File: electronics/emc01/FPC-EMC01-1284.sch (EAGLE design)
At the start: 75 parts, among them J1 USB-MINIB-5PIN, J11 CONN-RECT-16PIN-2ROW, J12 CONN-RECT-16PIN-2ROW, J13 CONN-RECT-16PIN-2ROW, J14 CONN-RECT-16PIN-2ROW, J15 DNP, J16 ICSP, J2 CONN-MOLEX-MICROFIT-6PIN, J3 DNP, J4A MOT-X, J5A MOT-Y, J6A MOT-Z, J7A CONN-RECT-3PINJST_PH_2MM, J8A CONN-RECT-3PINJST_PH_2MM, J9A CONN-RECT-3PINJST_PH_2MM, Q2 2N7002PW, U1 IC-ATMEGA1284P-AU, U2 FT231XS, X1 16Mhz

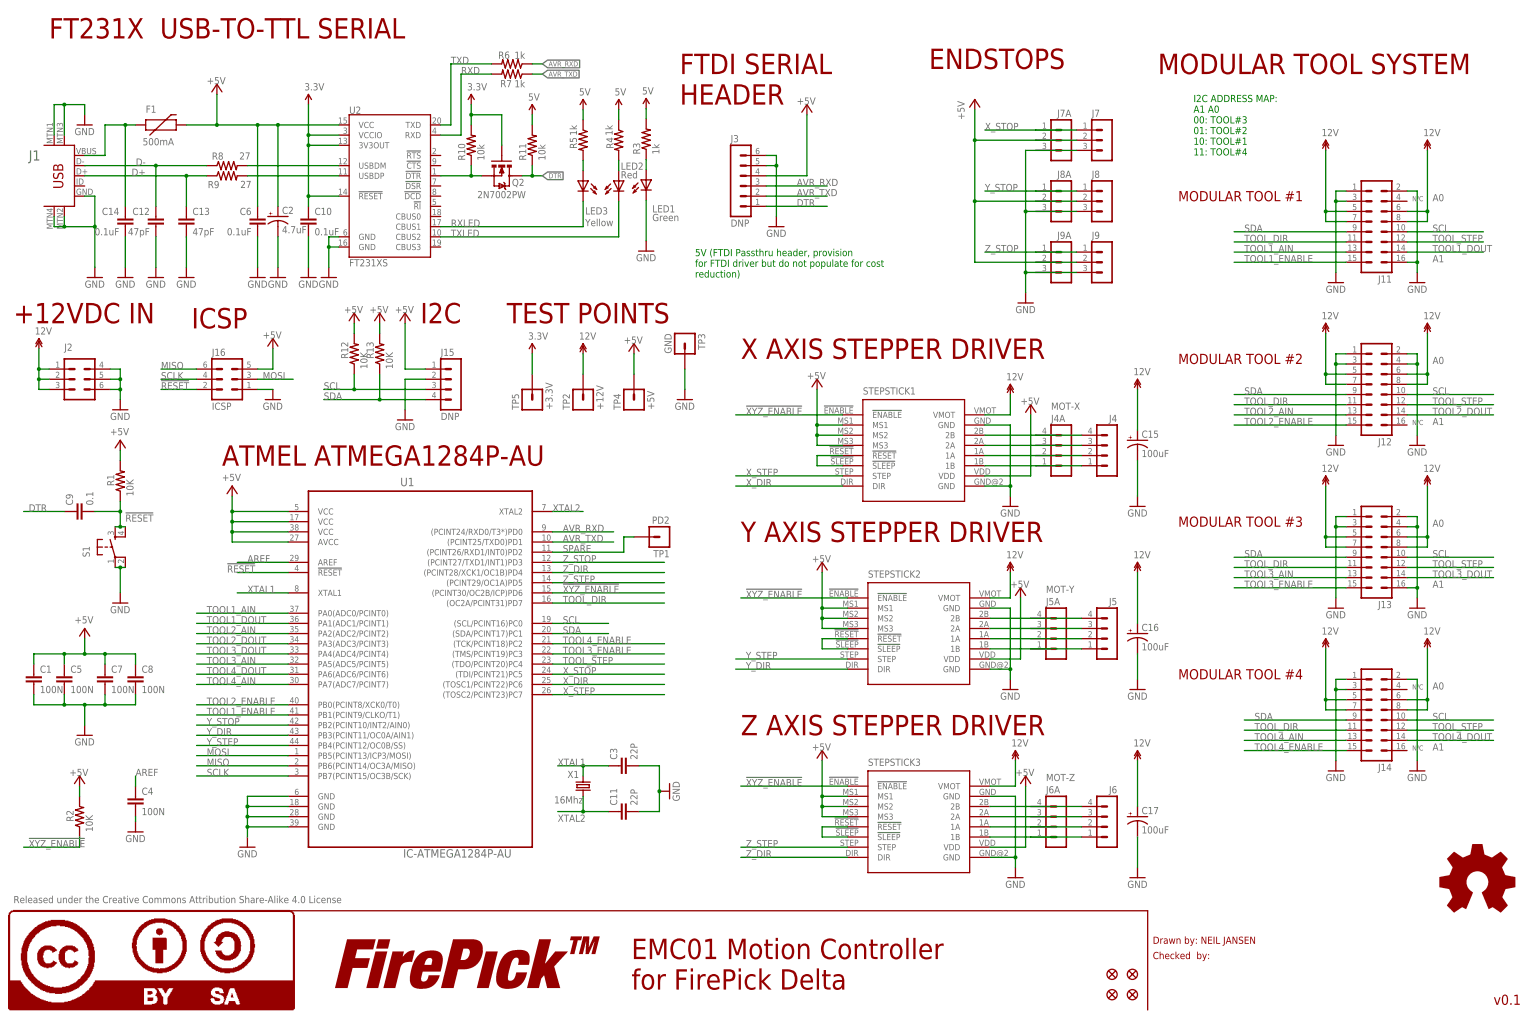
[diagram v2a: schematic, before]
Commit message: Updated all EAGLE PCB's for first Prototype production run.
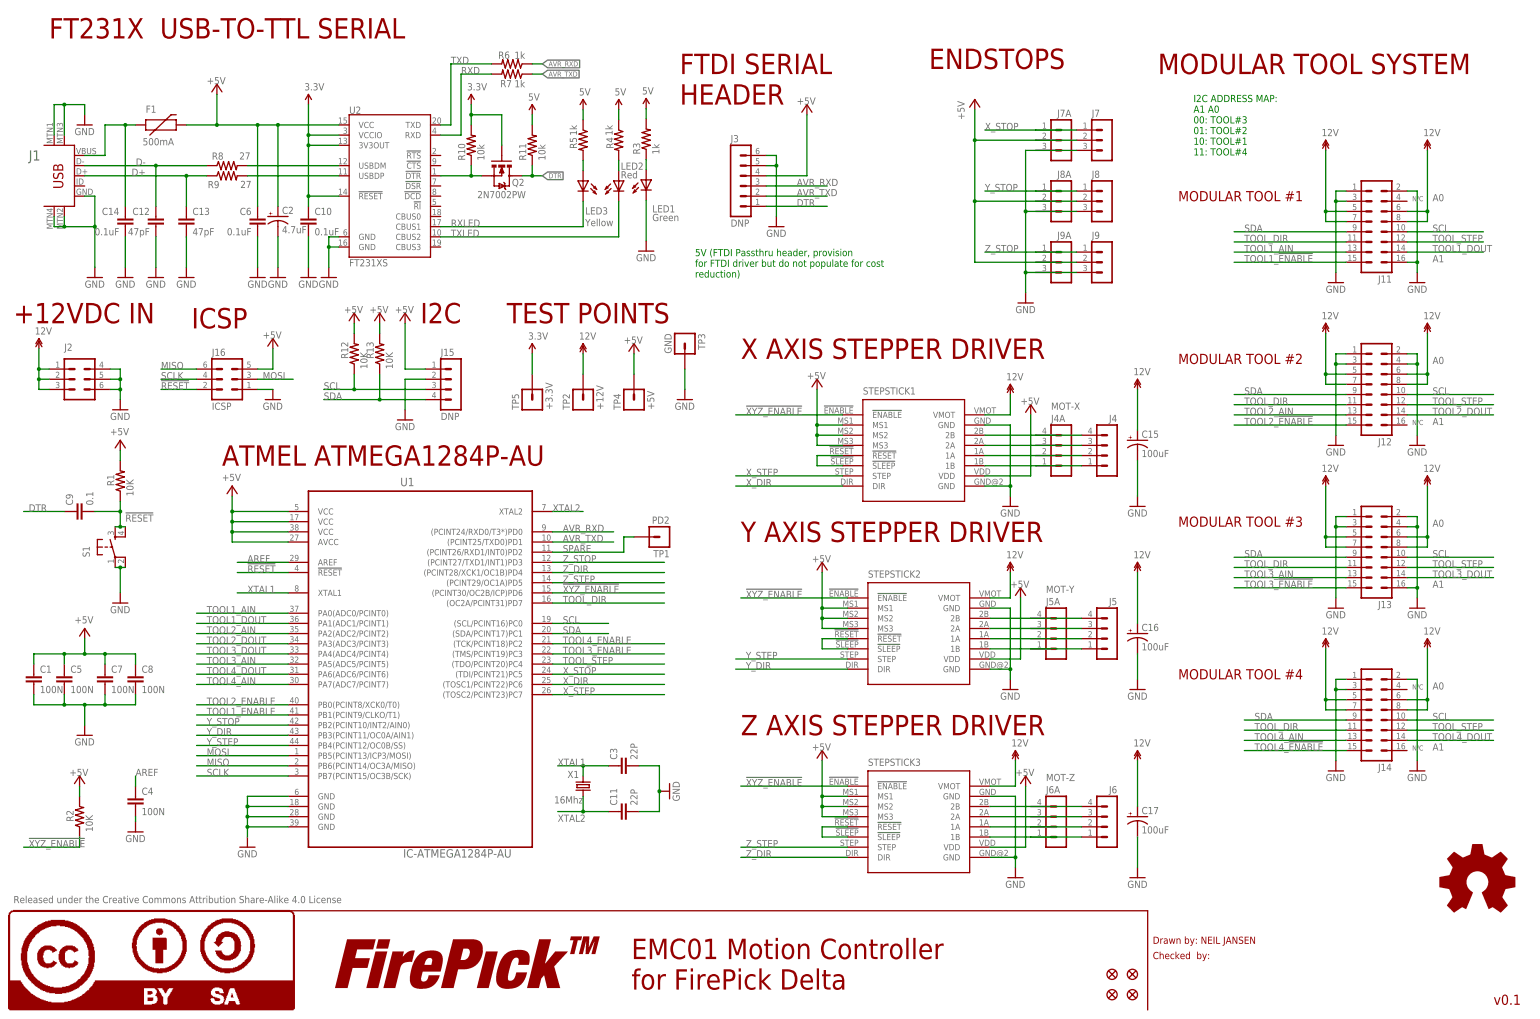
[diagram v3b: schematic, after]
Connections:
- new net TOOL1_!ENABLE: J11.15
- new net TOOL2_!ENABLE: J12.15
- new net TOOL3_!ENABLE: J13.15
- new net TOOL4_!ENABLE: J14.15
- net TOOL1_ENABLE: no longer J11.15
- net TOOL2_ENABLE: no longer J12.15
- net TOOL3_ENABLE: no longer J13.15
- net TOOL4_ENABLE: no longer J14.15
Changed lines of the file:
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@@
 <setting verticaltext="up"/>
 </settings>
-<grid distance="0.05" unitdist="inch" unit="inch" style="lines" multiple="1" display="no" altdistance="0.01" altunitdist="inch" altunit="inch"/>
+<grid distance="0.1" unitdist="inch" unit="inch" style="lines" multiple="1" display="no" altdistance="0.01" altunitdist="inch" altunit="inch"/>
 <layers>
 <layer number="1" name="Top" color="4" fill="1" visible="no" active="no"/>
@@
 <net name="TOOL1_ENABLE" class="0">
 <segment>
-<pinref part="J11" gate="G$1" pin="15"/>
-<wire x1="309.88" y1="190.5" x2="337.82" y2="190.5" width="0.1524" layer="91"/>
-<label x="312.42" y="190.5" size="1.778" layer="95"/>
-</segment>
-<segment>
 <pinref part="U1" gate="G$1" pin="PB1(PCINT9/CLKO/T1)"/>
 <wire x1="50.8" y1="77.47" x2="73.66" y2="77.47" width="0.1524" layer="91"/>
@@
 <net name="TOOL2_ENABLE" class="0">
 <segment>
-<pinref part="J12" gate="G$1" pin="15"/>
-<wire x1="337.82" y1="149.86" x2="309.88" y2="149.86" width="0.1524" layer="91"/>
-<label x="312.42" y="149.86" size="1.778" layer="95"/>
-</segment>
-<segment>
 <pinref part="U1" gate="G$1" pin="PB0(PCINT8/XCK0/T0)"/>
 <wire x1="73.66" y1="80.01" x2="50.8" y2="80.01" width="0.1524" layer="91"/>
@@
 <net name="TOOL3_ENABLE" class="0">
 <segment>
-<pinref part="J13" gate="G$1" pin="15"/>
-<wire x1="337.82" y1="109.22" x2="309.88" y2="109.22" width="0.1524" layer="91"/>
-<label x="312.42" y="109.22" size="1.778" layer="95"/>
-</segment>
-<segment>
 <pinref part="U1" gate="G$1" pin="(TMS/PCINT19)PC3"/>
 <wire x1="167.64" y1="92.71" x2="139.7" y2="92.71" width="0.1524" layer="91"/>
@@
 </net>
 <net name="TOOL4_ENABLE" class="0">
-<segment>
-<pinref part="J14" gate="G$1" pin="15"/>
-<wire x1="337.82" y1="68.58" x2="312.42" y2="68.58" width="0.1524" layer="91"/>
-<label x="314.96" y="68.58" size="1.778" layer="95"/>
-</segment>
 <segment>
 <pinref part="U1" gate="G$1" pin="(TCK/PCINT18)PC2"/>
@@
 <segment>
 <wire x1="73.66" y1="113.03" x2="60.96" y2="113.03" width="0.1524" layer="91"/>
-<label x="58.42" y="113.03" size="1.778" layer="95"/>
+<label x="63.5" y="113.03" size="1.778" layer="95"/>
 <pinref part="U1" gate="G$1" pin="!RESET"/>
 </segment>
@@
 </segment>
 </net>
+<net name="TOOL1_!ENABLE" class="0">
+<segment>
+<pinref part="J11" gate="G$1" pin="15"/>
+<wire x1="309.88" y1="190.5" x2="337.82" y2="190.5" width="0.1524" layer="91"/>
+<label x="312.42" y="190.5" size="1.778" layer="95"/>
+</segment>
+</net>
+<net name="TOOL2_!ENABLE" class="0">
+<segment>
+<pinref part="J12" gate="G$1" pin="15"/>
+<wire x1="337.82" y1="149.86" x2="309.88" y2="149.86" width="0.1524" layer="91"/>
+<label x="312.42" y="149.86" size="1.778" layer="95"/>
+</segment>
+</net>
+<net name="TOOL3_!ENABLE" class="0">
+<segment>
+<pinref part="J13" gate="G$1" pin="15"/>
+<wire x1="337.82" y1="109.22" x2="309.88" y2="109.22" width="0.1524" layer="91"/>
+<label x="312.42" y="109.22" size="1.778" layer="95"/>
+</segment>
+</net>
+<net name="TOOL4_!ENABLE" class="0">
+<segment>
+<pinref part="J14" gate="G$1" pin="15"/>
+<wire x1="337.82" y1="68.58" x2="312.42" y2="68.58" width="0.1524" layer="91"/>
+<label x="314.96" y="68.58" size="1.778" layer="95"/>
+</segment>
+</net>

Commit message: REVISION A of EMC01 board.  Fixed unconnected wires on TOOL1_ENABLE, TOOL2_ENABLE, TOOL3_ENABLE, and TOOL4_ENABLE.  This was discovered by Seeed Studio Fusion PCB service after being submitted to be manufactured.
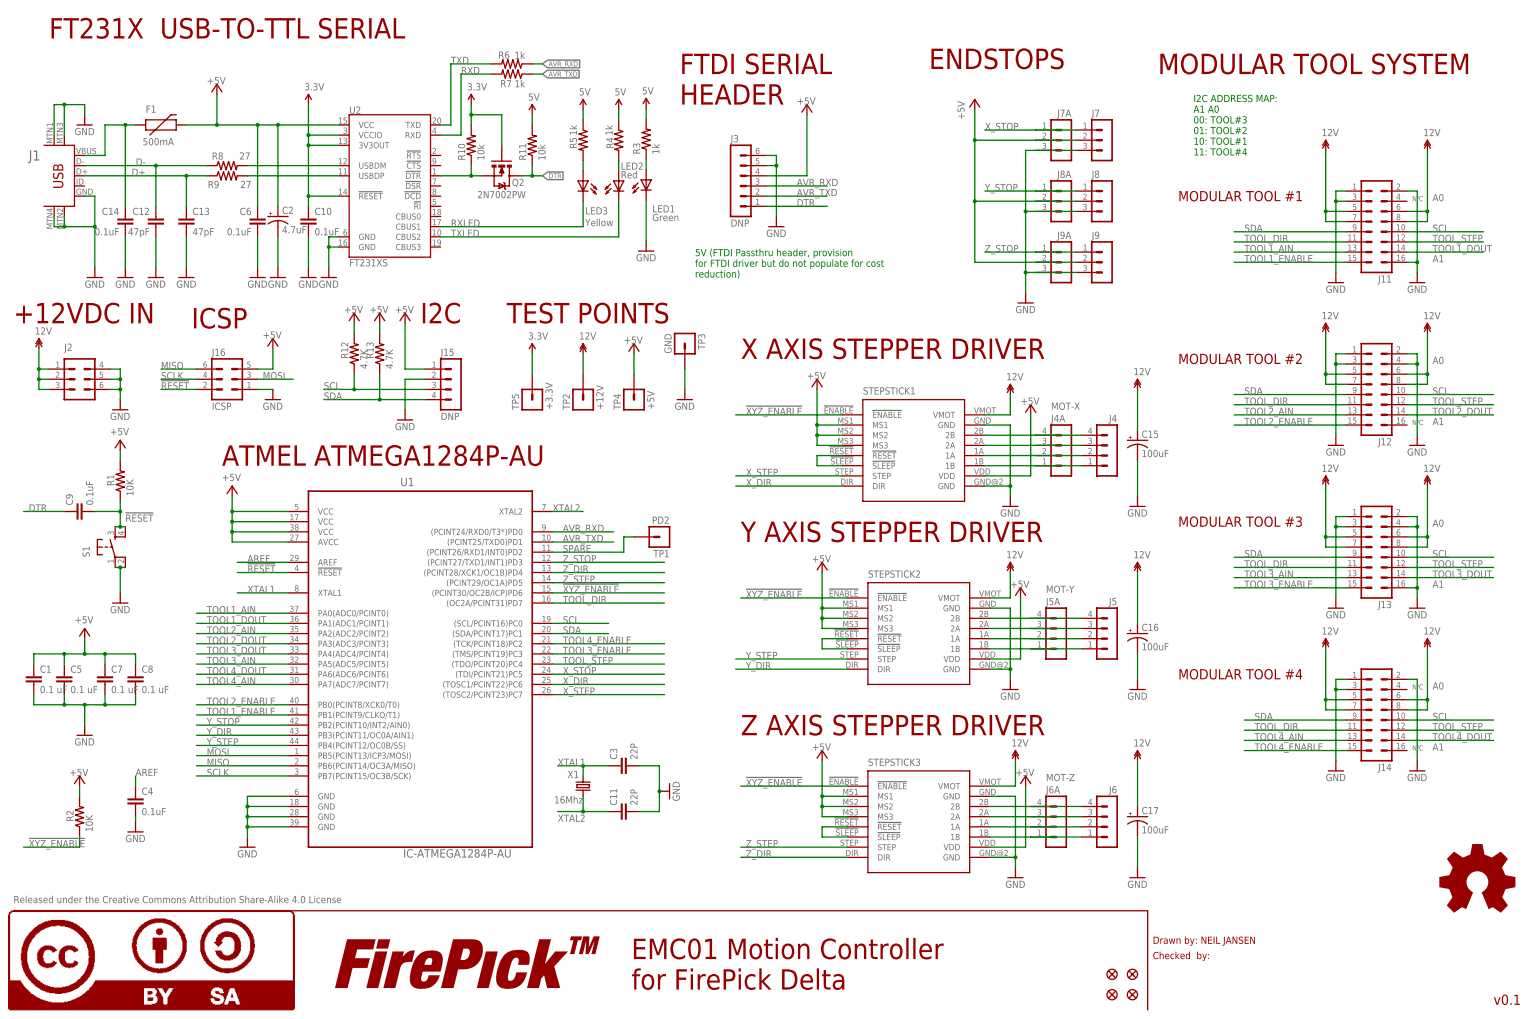
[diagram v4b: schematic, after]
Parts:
- C1, C5, C7, C8: value 100N -> 0.1 uF
- C4: value 100N -> 0.1uF
- C9: value 0.1 -> 0.1uF
- R12, R13: value 10K -> 4.7K
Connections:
- removed net TOOL1_!ENABLE: J11.15
- removed net TOOL2_!ENABLE: J12.15
- removed net TOOL3_!ENABLE: J13.15
- removed net TOOL4_!ENABLE: J14.15
- net TOOL1_ENABLE: now also J11.15
- net TOOL2_ENABLE: now also J12.15
- net TOOL3_ENABLE: now also J13.15
- net TOOL4_ENABLE: now also J14.15
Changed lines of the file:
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@@
 <part name="J5" library="!con-lstb" deviceset="MA04-1" device=""/>
 <part name="J6" library="!con-lstb" deviceset="MA04-1" device=""/>
-<part name="C1" library="SparkFun-Capacitors" deviceset="CAP" device="0805" value="100N"/>
-<part name="C5" library="SparkFun-Capacitors" deviceset="CAP" device="0805" value="100N"/>
-<part name="C7" library="SparkFun-Capacitors" deviceset="CAP" device="0805" value="100N"/>
-<part name="C8" library="SparkFun-Capacitors" deviceset="CAP" device="0805" value="100N"/>
-<part name="C9" library="SparkFun-Capacitors" deviceset="CAP" device="0805" value="0.1"/>
+<part name="C1" library="SparkFun-Capacitors" deviceset="CAP" device="0805" value="0.1 uF"/>
+<part name="C5" library="SparkFun-Capacitors" deviceset="CAP" device="0805" value="0.1 uF"/>
+<part name="C7" library="SparkFun-Capacitors" deviceset="CAP" device="0805" value="0.1 uF"/>
+<part name="C8" library="SparkFun-Capacitors" deviceset="CAP" device="0805" value="0.1 uF"/>
+<part name="C9" library="SparkFun-Capacitors" deviceset="CAP" device="0805" value="0.1uF"/>
 <part name="GND11" library="supply1" deviceset="GND" device=""/>
 <part name="P+10" library="supply1" deviceset="+5V" device=""/>
 <part name="C3" library="SparkFun-Capacitors" deviceset="CAP" device="0805" value="22P"/>
 <part name="C11" library="SparkFun-Capacitors" deviceset="CAP" device="0805" value="22P"/>
-<part name="C4" library="SparkFun-Capacitors" deviceset="CAP" device="0805" value="100N"/>
+<part name="C4" library="SparkFun-Capacitors" deviceset="CAP" device="0805" value="0.1uF"/>
 <part name="C2" library="rcl" deviceset="CPOL-US" device="D" value="4.7uF"/>
 <part name="U1" library="FirePick" deviceset="IC-ATMEGA1284P-AU" device=""/>
@@
 <part name="LOGO5" library="FirePick" deviceset="LOGO-OSHW" device="MEDIUM"/>
 <part name="LOGO6" library="FirePick" deviceset="LOGO-CC-BY-SA" device=""/>
-<part name="R12" library="SparkFun-Resistors" deviceset="RESISTOR" device="0805-RES" value="10K"/>
-<part name="R13" library="SparkFun-Resistors" deviceset="RESISTOR" device="0805-RES" value="10K"/>
+<part name="R12" library="SparkFun-Resistors" deviceset="RESISTOR" device="0805-RES" value="4.7K"/>
+<part name="R13" library="SparkFun-Resistors" deviceset="RESISTOR" device="0805-RES" value="4.7K"/>
 <part name="P+6" library="supply1" deviceset="+5V" device=""/>
 <part name="P+7" library="supply1" deviceset="+5V" device=""/>
@@
 <label x="53.34" y="77.47" size="1.778" layer="95"/>
 </segment>
+<segment>
+<pinref part="J11" gate="G$1" pin="15"/>
+<wire x1="309.88" y1="190.5" x2="337.82" y2="190.5" width="0.1524" layer="91"/>
+<label x="312.42" y="190.5" size="1.778" layer="95"/>
+</segment>
 </net>
 <net name="TOOL2_ENABLE" class="0">
@@
 <label x="53.34" y="80.01" size="1.778" layer="95"/>
 </segment>
+<segment>
+<pinref part="J12" gate="G$1" pin="15"/>
+<wire x1="337.82" y1="149.86" x2="309.88" y2="149.86" width="0.1524" layer="91"/>
+<label x="312.42" y="149.86" size="1.778" layer="95"/>
+</segment>
 </net>
 <net name="TOOL2_AIN" class="0">
@@
 <label x="142.24" y="92.71" size="1.778" layer="95"/>
 </segment>
+<segment>
+<pinref part="J13" gate="G$1" pin="15"/>
+<wire x1="337.82" y1="109.22" x2="309.88" y2="109.22" width="0.1524" layer="91"/>
+<label x="312.42" y="109.22" size="1.778" layer="95"/>
+</segment>
 </net>
 <net name="TOOL3_AIN" class="0">
@@
 <wire x1="139.7" y1="95.25" x2="167.64" y2="95.25" width="0.1524" layer="91"/>
 <label x="142.24" y="95.25" size="1.778" layer="95"/>
+</segment>
+<segment>
+<pinref part="J14" gate="G$1" pin="15"/>
+<wire x1="337.82" y1="68.58" x2="312.42" y2="68.58" width="0.1524" layer="91"/>
+<label x="314.96" y="68.58" size="1.778" layer="95"/>
 </segment>
 </net>
@@
 </segment>
 </net>
-<net name="TOOL1_!ENABLE" class="0">
-<segment>
-<pinref part="J11" gate="G$1" pin="15"/>
-<wire x1="309.88" y1="190.5" x2="337.82" y2="190.5" width="0.1524" layer="91"/>
-<label x="312.42" y="190.5" size="1.778" layer="95"/>
-</segment>
-</net>
-<net name="TOOL2_!ENABLE" class="0">
-<segment>
-<pinref part="J12" gate="G$1" pin="15"/>
-<wire x1="337.82" y1="149.86" x2="309.88" y2="149.86" width="0.1524" layer="91"/>
-<label x="312.42" y="149.86" size="1.778" layer="95"/>
-</segment>
-</net>
-<net name="TOOL3_!ENABLE" class="0">
-<segment>
-<pinref part="J13" gate="G$1" pin="15"/>
-<wire x1="337.82" y1="109.22" x2="309.88" y2="109.22" width="0.1524" layer="91"/>
-<label x="312.42" y="109.22" size="1.778" layer="95"/>
-</segment>
-</net>
-<net name="TOOL4_!ENABLE" class="0">
-<segment>
-<pinref part="J14" gate="G$1" pin="15"/>
-<wire x1="337.82" y1="68.58" x2="312.42" y2="68.58" width="0.1524" layer="91"/>
-<label x="314.96" y="68.58" size="1.778" layer="95"/>
-</segment>
-</net>

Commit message: EMC01 Revision B: Added +5V voltage regulator and other misc stuff
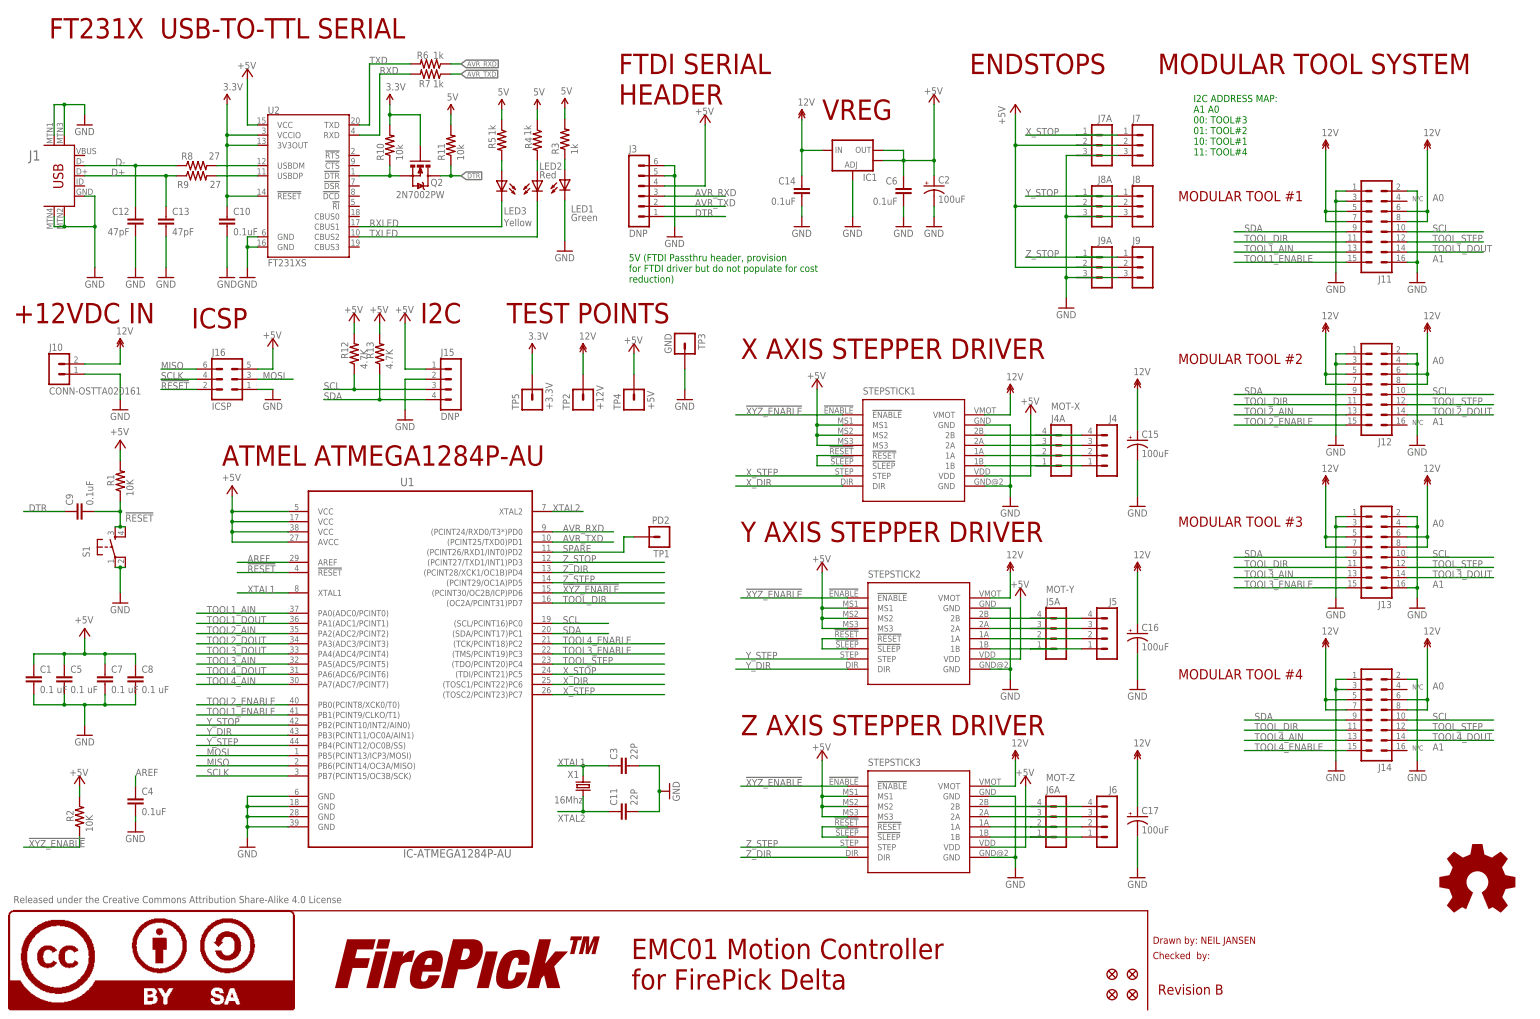
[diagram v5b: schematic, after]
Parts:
- removed F1: 500mA, SparkFun:PTCSMD
- removed J2: CONN-MOLEX-MICROFIT-6PIN, FirePick:CONN-MOLEX-MICROFIT-6PIN
- added IC1: (no value), SparkFun-PowerIC:V_REG_LM1117SOT223
- added J10: CONN-OSTTA020161, FirePick:CONN-OSTTA020161
- C2: value 4.7uF -> 100uF
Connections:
- removed net VUSB: C14.1, F1.1, J1.VBUS
- net +5V: now also IC1.OUT, IC1.OUT@1; no longer F1.2
- net 12V: now also C14.1, IC1.IN, J10.2; no longer J2.1, J2.2, J2.3
- net GND: now also IC1.ADJ, J10.1; no longer J2.4, J2.5, J2.6
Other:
- note added: "Revision B"
- note added: "VREG"
- note removed: "v0.1"
- moved on the sheet: C10, C12, C13, C14, C2, C6, J3, J7, J7A, J8, J8A, J9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
